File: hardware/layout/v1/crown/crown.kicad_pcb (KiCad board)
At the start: 4 copper layers, 34 x 34 mm, 47 parts, among them J1 Main board, J10 DOME_SOCKET, J2 XD_North, J3 XD_East, J4 XD_South, J5 XD_West, J6 PIEZO_NE, J7 PIEZO_NW, J8 PIEZO_SW, J9 PIEZO_SE, U1 SN74LVC2G04DBVR, U2 CD4052BM96, U3 TLV9062IDR, U4 LM393DR2G, U5 TLV9062IDR, U6 MMC5603NJ

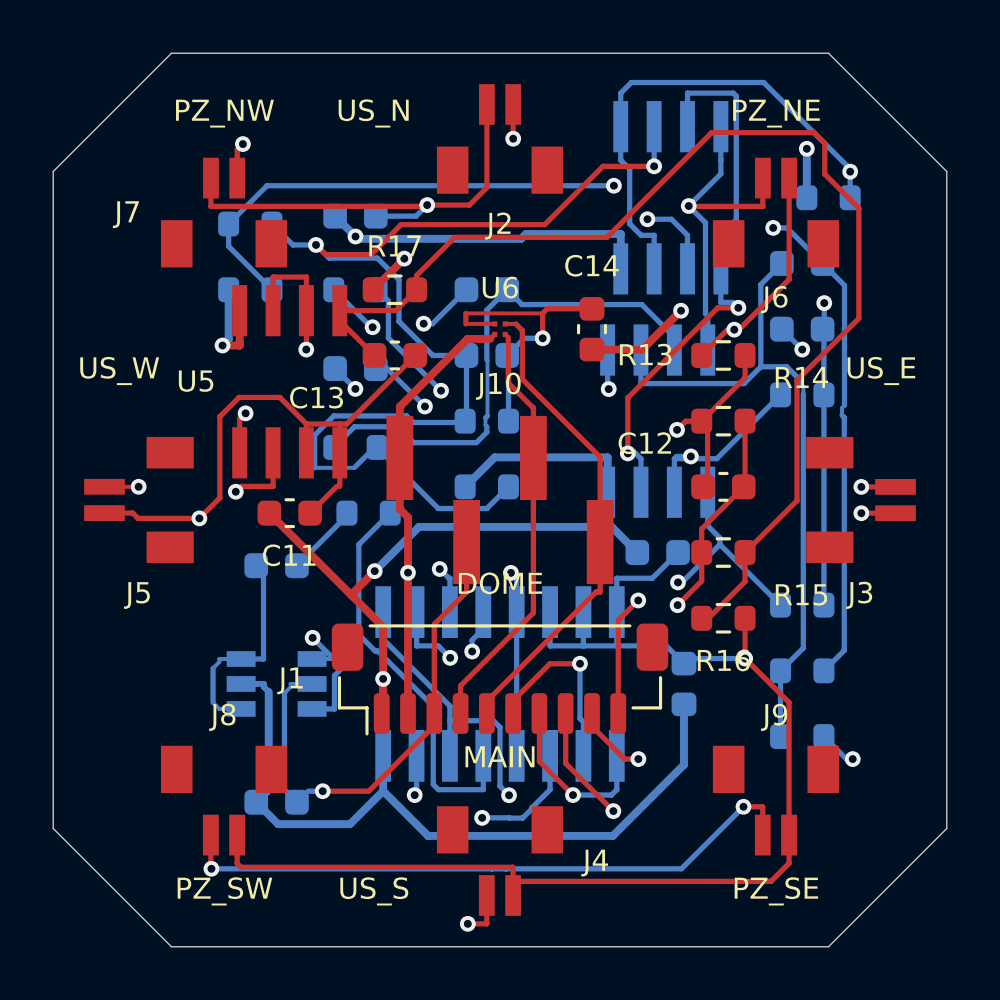
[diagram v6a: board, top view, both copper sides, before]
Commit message: Update enclosure dimensions, add power board, upgrade sensors, and redesign base bay for PMSA003I particulate module
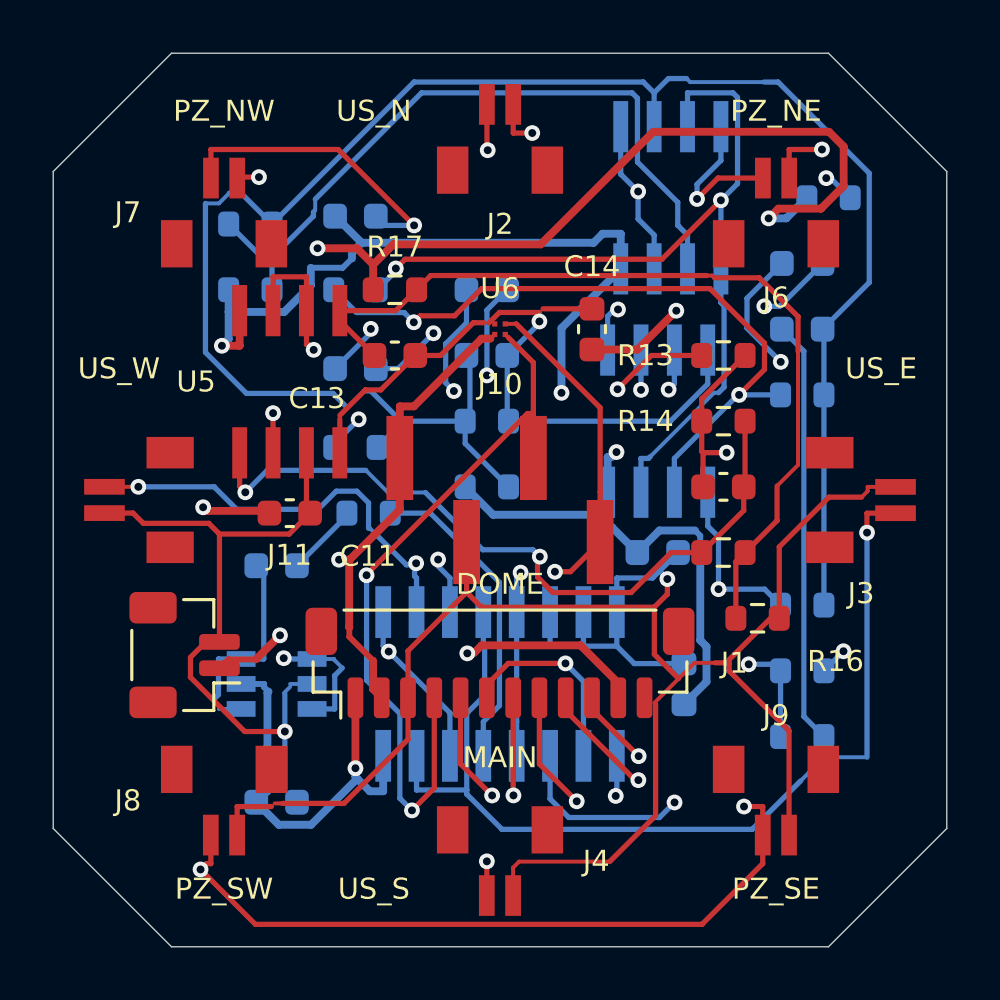
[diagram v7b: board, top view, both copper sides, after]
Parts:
- added J11: AUX 5V_HEAT, Connector_JST:JST_SH_BM02B-SRSS-TB_1x02-1MP_P1.00mm_Vertical, F.Cu at (5.00, -11.1)
- J1: footprint Connector_JST:JST_SH_BM10B-SRSS-TB_1x10-1MP_P1.00mm_Vertical -> Connector_JST:JST_SH_BM12B-SRSS-TB_1x12-1MP_P1.00mm_Vertical
- moved R16 1.30 mm to (26.8, -12.5)
- moved J1 0.60 mm to (17.0, -10.8)
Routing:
- net PIEZO_IN: track 85.6 -> 105.8 mm, vias 4 -> 5
- net +5V_HEAT: track 0.00 -> 17.3 mm, vias 0 -> 2
- net GND: track 131.6 -> 145.5 mm, vias 7 -> 6
- net +3V3: track 57.9 -> 71.1 mm
- net US_AMP1_FB: track 26.0 -> 39.2 mm, vias 0 -> 3
- net US_AMP2_IN: track 22.5 -> 35.7 mm
- net I2C_SDA: track 16.0 -> 28.4 mm, vias 0 -> 2
- net PIEZO_ENV: track 45.2 -> 33.3 mm
- net +5V: track 100.5 -> 90.2 mm, vias 4 -> 5
- net US_RX: track 47.3 -> 55.7 mm, vias 2 -> 3
- net I2C_SCL: track 18.4 -> 26.0 mm, vias 0 -> 2
- net XD_W: track 35.7 -> 41.4 mm
- net N$2: track 21.9 -> 16.2 mm, vias 2 -> 0
- net PIEZO_INV: track 37.4 -> 32.4 mm
- net US_AMP1_OUT: track 44.9 -> 39.9 mm, vias 3 -> 4
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
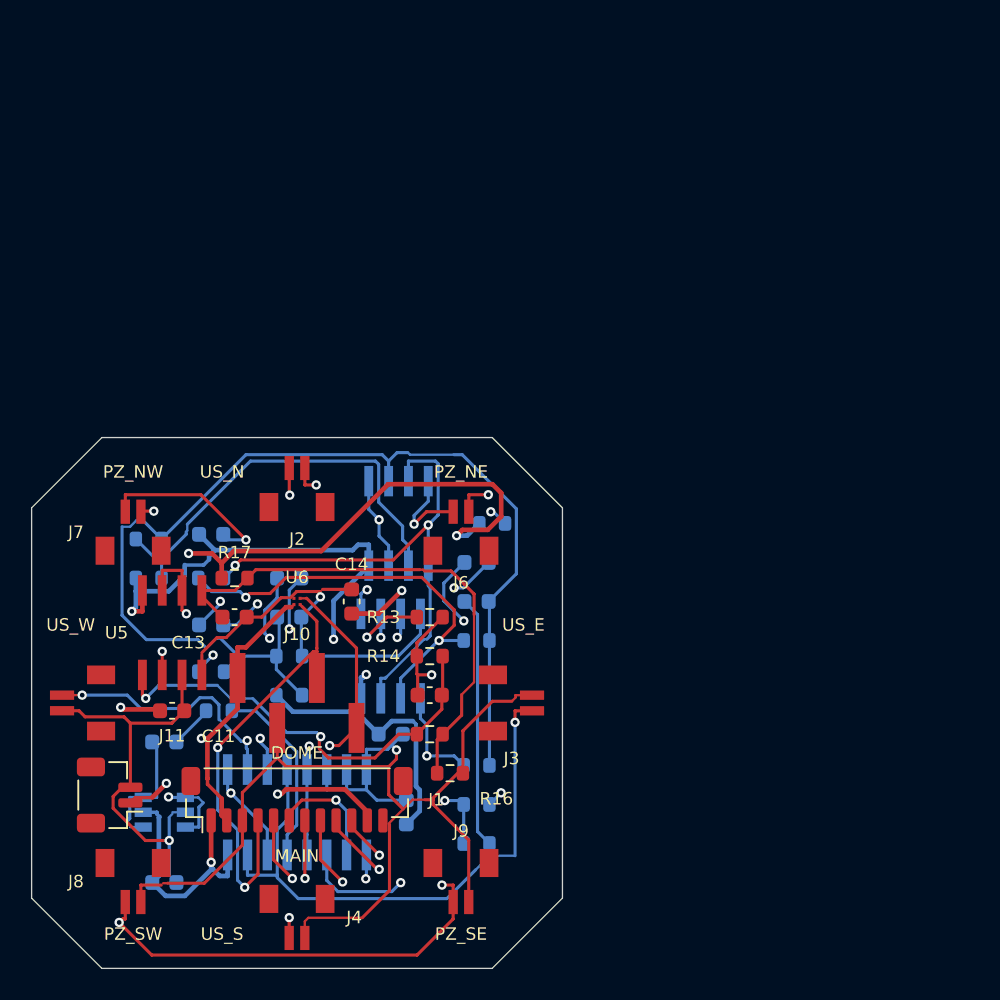
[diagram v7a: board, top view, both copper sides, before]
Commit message: Update documentation for 60V power system, STM32 crown board, 12V heaters, and expanded enclosure design
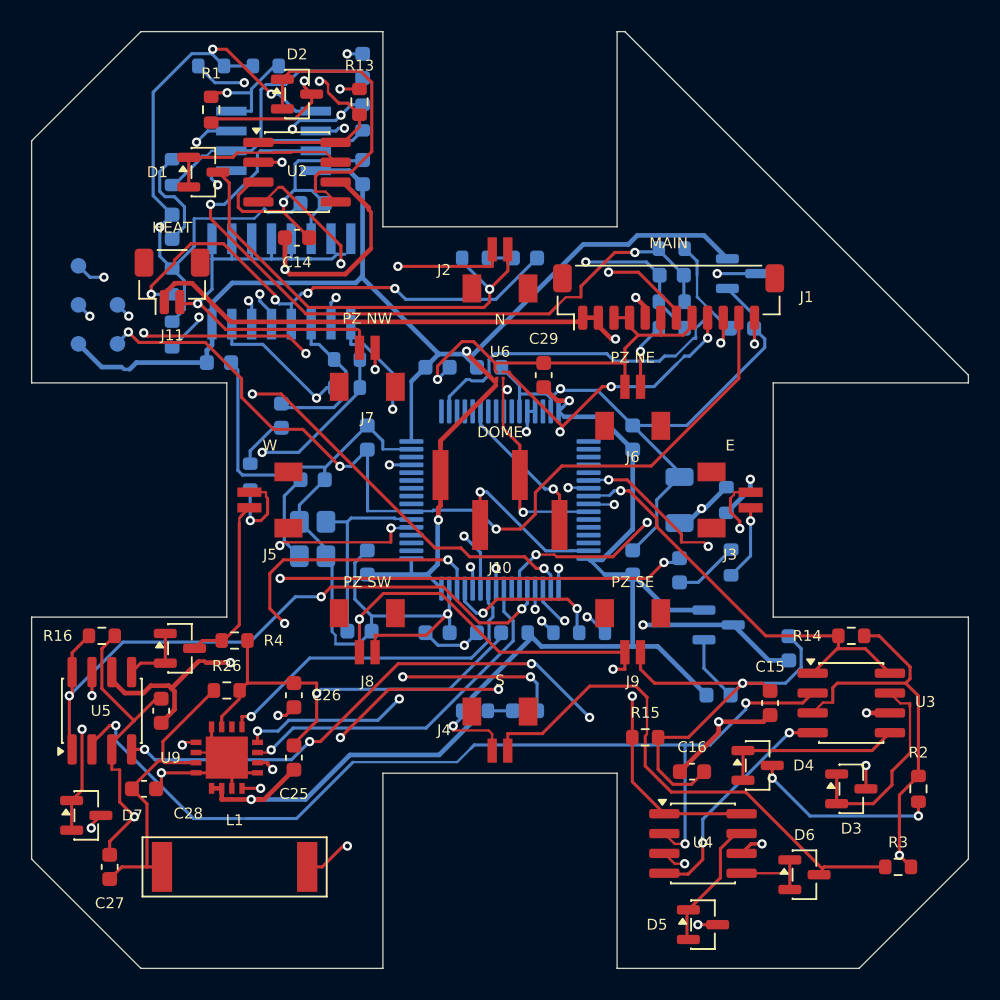
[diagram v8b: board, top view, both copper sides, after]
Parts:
- added C15: 1u 50V, Capacitor_SMD:C_0603_1608Metric, F.Cu at (47.3, -17.0)
- added C16: 1u 50V, Capacitor_SMD:C_0603_1608Metric, F.Cu at (42.3, -12.6)
- added C17: 1u 50V, Capacitor_SMD:C_0603_1608Metric, F.Cu at (8.30, -16.5)
- added C18: 1u 50V, Capacitor_SMD:C_0603_1608Metric, B.Cu at (18.0, -49.0)
- added C19: 100n 50V, Capacitor_SMD:C_0603_1608Metric, B.Cu at (9.00, -47.5)
- added C20: 220p C0G 50V, Capacitor_SMD:C_0603_1608Metric, B.Cu at (21.2, -57.8)
- added C21: 22n 50V, Capacitor_SMD:C_0603_1608Metric, B.Cu at (41.0, -44.4)
- added C22: 1n 50V, Capacitor_SMD:C_0603_1608Metric, B.Cu at (45.5, -41.0)
- added C23: 100n 50V, Capacitor_SMD:C_0603_1608Metric, B.Cu at (21.2, -51.0)
- added C24: 100n 50V, Capacitor_SMD:C_0603_1608Metric, B.Cu at (12.0, -38.8)
- added C25: 100n 50V, Capacitor_SMD:C_0603_1608Metric, F.Cu at (16.8, -13.5)
- added C26: 1u 50V, Capacitor_SMD:C_0603_1608Metric, F.Cu at (16.8, -17.5)
- added C27: 470p C0G 50V, Capacitor_SMD:C_0603_1608Metric, F.Cu at (5.00, -6.50)
- added C28: 470p C0G 50V, Capacitor_SMD:C_0603_1608Metric, F.Cu at (7.20, -11.5)
- added C29: 100n 50V, Capacitor_SMD:C_0603_1608Metric, F.Cu at (32.8, -38.0)
- added C30: 10n 50V, Capacitor_SMD:C_0603_1608Metric, B.Cu at (31.6, -45.5)
- added C31: 10n 50V, Capacitor_SMD:C_0603_1608Metric, B.Cu at (41.5, -25.5)
- added C32: 10n 50V, Capacitor_SMD:C_0603_1608Metric, B.Cu at (31.6, -16.5)
- added C33: 10n 50V, Capacitor_SMD:C_0603_1608Metric, B.Cu at (16.0, -35.4)
- added D1: BAV99, Package_TO_SOT_SMD:SOT-23, F.Cu at (11.0, -51.0)
- added D2: BAV99, Package_TO_SOT_SMD:SOT-23, F.Cu at (17.0, -56.0)
- added D3: BAV99, Package_TO_SOT_SMD:SOT-23, F.Cu at (52.5, -11.5)
- added D4: BAV99, Package_TO_SOT_SMD:SOT-23, F.Cu at (46.5, -13.0)
- added D5: BAV99, Package_TO_SOT_SMD:SOT-23, F.Cu at (43.0, -2.80)
- added D6: BAV99, Package_TO_SOT_SMD:SOT-23, F.Cu at (49.5, -6.00)
- added D7: BAV99, Package_TO_SOT_SMD:SOT-23, F.Cu at (3.50, -9.80)
- added D8: BAV99, Package_TO_SOT_SMD:SOT-23, F.Cu at (9.50, -20.5)
- added D9: BAV99, Package_TO_SOT_SMD:SOT-23, B.Cu at (45.5, -44.5)
- added L1: 100uH, RF_Antenna:Coilcraft_MA5532-AE_RFID, F.Cu at (13.0, -6.50)
- added R18: 10k, Resistor_SMD:R_0603_1608Metric, B.Cu at (11.5, -57.8)
- added R19: 10k, Resistor_SMD:R_0603_1608Metric, B.Cu at (15.0, -57.8)
- added R20: 1k, Resistor_SMD:R_0603_1608Metric, B.Cu at (9.00, -51.0)
- added R21: 6k8, Resistor_SMD:R_0603_1608Metric, B.Cu at (21.2, -54.5)
- added R22: 1k, Resistor_SMD:R_0603_1608Metric, B.Cu at (41.0, -41.0)
- added R23: 4M7, Resistor_SMD:R_0603_1608Metric, B.Cu at (41.0, -42.7)
- added R24: 1k, Resistor_SMD:R_0603_1608Metric, B.Cu at (41.0, -46.1)
- added R25: 10k, Resistor_SMD:R_0603_1608Metric, B.Cu at (35.9, -21.5)
- added R26: 10k, Resistor_SMD:R_0603_1608Metric, F.Cu at (12.5, -17.8)
- added R27: 10R, Resistor_SMD:R_0603_1608Metric, B.Cu at (32.6, -21.5)
- added TP1: 3V3, TestPoint:TestPoint_Pad_D1.0mm, B.Cu at (3.00, -40.0)
- added TP2: SWDIO, TestPoint:TestPoint_Pad_D1.0mm, B.Cu at (3.00, -42.5)
- added TP3: SWCLK, TestPoint:TestPoint_Pad_D1.0mm, B.Cu at (3.00, -45.0)
- added TP4: NRST, TestPoint:TestPoint_Pad_D1.0mm, B.Cu at (5.50, -40.0)
- added TP5: GND, TestPoint:TestPoint_Pad_D1.0mm, B.Cu at (5.50, -42.5)
- added U10: XC6206P332MR, Package_TO_SOT_SMD:SOT-23, B.Cu at (44.0, -22.0)
- added U7: 74HC4052D, gateway_fp:TI_CD4052BM96_SOIC-16, B.Cu at (16.0, -44.0)
- added U8: TLV9062IDR, gateway_fp:TI_TLV9062IDR_SOIC-8, B.Cu at (15.5, -53.0)
- added U9: AS3935-BQFT, gateway_fp:ScioSense_AS3935_QFN-16, F.Cu at (12.5, -13.5)
- added Y1: 8MHz, Crystal:Crystal_SMD_3225-4Pin_3.2x2.5mm, B.Cu at (18.0, -27.5)
- C1, C14: value 100n 50V -> 1u 50V
- C11: value 100n 50V -> 33p C0G 50V; moved to B.Cu
- C12: value 18p C0G 50V -> 33p C0G 50V; moved to B.Cu
- C13: value 220n 50V -> 22u 25V; footprint Capacitor_SMD:C_0603_1608Metric -> Capacitor_SMD:C_1206_3216Metric; moved to B.Cu
- C2: value 100n 50V -> 10u 10V
- C6, C9: value 47n 50V -> 100n 50V
- C7: value 47n 50V -> 10u 10V
- C8: value 18p C0G 50V -> 1u 50V
- J11: value AUX 5V_HEAT -> AUX 12V_HEAT
- J2: value XD_North -> XD_N
- J3: value XD_East -> XD_E
- J4: value XD_South -> XD_S
- J5: value XD_West -> XD_W
- R1, R4: value 1k -> 330R; moved to F.Cu
- R10: value 100k -> 1M
- R11: value 10k -> 1M
- R12: value 4k7 -> 1M
- R13: value 1k -> 10k
- R14: value 100k -> 10k
- R16: value 20k -> 10k
- R17: value 100k -> 10R; moved to B.Cu
- R2, R3: value 10k -> 330R; moved to F.Cu
- R5, R8: value 1k -> 47k
- R6: value 22k -> 47k
- R7: value 10k -> 47k
- R9: value 22k -> 1M
- U1: value SN74LVC2G04DBVR -> STM32G431RBT6; footprint gateway_fp:TI_SN74LVC2G04_SOT-23-6 -> Package_QFP:LQFP-64_10x10mm_P0.5mm
- U2: value CD4052BM96 -> UCC27524ADR; footprint gateway_fp:TI_CD4052BM96_SOIC-16 -> Package_SO:SOIC-8_3.9x4.9mm_P1.27mm; moved to F.Cu
- U3: value TLV9062IDR -> UCC27524ADR; footprint gateway_fp:TI_TLV9062IDR_SOIC-8 -> Package_SO:SOIC-8_3.9x4.9mm_P1.27mm; moved to F.Cu
- U4: value LM393DR2G -> UCC27524ADR; footprint gateway_fp:ON_LM393DR2G_SOIC-8 -> Package_SO:SOIC-8_3.9x4.9mm_P1.27mm; moved to F.Cu
- U5: value TLV9062IDR -> UCC27524ADR; footprint gateway_fp:TI_TLV9062IDR_SOIC-8 -> Package_SO:SOIC-8_3.9x4.9mm_P1.27mm
- moved C1 42.7 mm to (48.5, -20.5), turned to 90 degrees
- moved R3 41.3 mm to (55.5, -6.50)
- moved U2 41.0 mm to (17.0, -51.0)
- moved R2 40.7 mm to (56.8, -11.5), turned to 90 degrees
- moved J1 40.0 mm to (40.8, -43.0)
- moved R1 38.5 mm to (11.5, -55.0), turned to 90 degrees
- moved R5 37.5 mm to (28.4, -45.5)
- moved C2 35.6 mm to (44.0, -17.5)
- moved R13 33.3 mm to (21.0, -55.5), turned to 90 degrees
- moved J11 33.1 mm to (9.00, -44.0), turned to 0 degrees
- moved R17 31.9 mm to (44.5, -30.0), turned to 90 degrees
- moved U3 29.7 mm to (52.5, -17.0)
- moved C13 29.5 mm to (41.5, -30.0), turned to 90 degrees
- moved U1 29.4 mm to (30.0, -30.0)
- moved U4 28.3 mm to (43.0, -8.00)
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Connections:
- C10 pad 1: +5V -> CROWN_NRST
- C11 pad 1: +5V -> XTAL_IN
- C12 pad 1: PIEZO_INV -> XTAL_OUT
- C12 pad 2: PIEZO_STG1 -> GND
- C13 pad 1: PIEZO_ENV -> VDRV
- C14 pad 1: +3V3 -> VDRV
- C2 pad 1: US_TX_DRV -> +3V3
- C2 pad 2: N$1 -> GND
- C3 pad 1: +5V -> +3V3
- C4 pad 1: US_VREF -> +3V3
- C5 pad 1: +5V -> +3V3
- C6 pad 1: US_RX_MUX -> +3V3
- C6 pad 2: US_AMP1_IN -> GND
- C7 pad 1: N$2 -> +3V3
- C7 pad 2: US_VREF -> GND
- C8 pad 1: US_AMP1_FB -> +3V3A
- C8 pad 2: US_AMP1_OUT -> GND
- C9 pad 1: US_AMP1_OUT -> +3V3A
- C9 pad 2: US_AMP2_IN -> GND
- J1 pad 1: +5V -> +12V_HEAT
- J1 pad 10: RAIN_ADC -> CROWN_IRQ
- J1 pad 11: +5V_HEAT -> CROWN_NRST
- J1 pad 12: GND -> CROWN_BOOT0
- J1 pad 2: +3V3 -> +12V_HEAT
- J1 pad 4: I2C_SDA -> GND
- J1 pad 5: I2C_SCL -> +5V
- J1 pad 6: US_SEL_A -> GND
- J1 pad 7: US_SEL_B -> I2C_SDA
- J1 pad 8: US_TX -> GND
- J1 pad 9: US_RX -> I2C_SCL
- J11 pad 1: +5V_HEAT -> +12V_HEAT
- J2 pad 1: XD_N -> XD_N_A
- J2 pad 2: GND -> XD_N_B
- J3 pad 1: XD_E -> XD_E_A
- J3 pad 2: GND -> XD_E_B
- J4 pad 1: XD_S -> XD_S_A
- J4 pad 2: GND -> XD_S_B
- J5 pad 1: XD_W -> XD_W_A
- J5 pad 2: GND -> XD_W_B
- R1 pad 1: N$1 -> XD_N_B
- R1 pad 2: US_TX_AC -> GND
- R10 pad 1: +5V -> XD_E_RX
- R10 pad 2: US_VTH -> US_VREF
- R11 pad 1: US_VTH -> XD_S_RX
- R12 pad 1: +3V3 -> XD_W_RX
- R12 pad 2: US_RX -> US_VREF
- R13 pad 1: PIEZO_IN -> XD_EN_N
- R13 pad 2: PIEZO_INV -> GND
- R14 pad 1: PIEZO_INV -> XD_EN_E
- R14 pad 2: PIEZO_STG1 -> GND
- R15 pad 1: PIEZO_STG1 -> XD_EN_S
- R15 pad 2: PIEZO_ENV -> GND
- R16 pad 1: PIEZO_ENV -> XD_EN_W
- R17 pad 1: +3V3 -> +12V_HEAT
- R17 pad 2: PIEZO_ENV -> VDRV
- R2 pad 1: +5V -> XD_E_B
- R2 pad 2: US_VREF -> GND
- R3 pad 1: US_VREF -> XD_S_B
- R4 pad 1: US_AMP1_IN -> XD_W_B
- R4 pad 2: US_VREF -> GND
- R5 pad 1: US_AMP1_FB -> XD_N_A
- R5 pad 2: N$2 -> XD_N_RXC
- R6 pad 1: US_AMP1_FB -> XD_E_A
- R6 pad 2: US_AMP1_OUT -> XD_E_RXC
- R7 pad 1: US_AMP2_IN -> XD_S_A
- R7 pad 2: US_VREF -> XD_S_RXC
- R8 pad 1: US_AMP2_FB -> XD_W_A
- R8 pad 2: US_VREF -> XD_W_RXC
- R9 pad 1: US_AMP2_FB -> XD_N_RX
- R9 pad 2: US_AMP2_OUT -> US_VREF
- U1 pad 1: US_TX -> +3V3
- U1 pad 2: GND -> (no net)
- U1 pad 3: US_TX -> (no net)
- U1 pad 4: US_TX_DRV -> (no net)
- U1 pad 5: +5V -> XTAL_IN
- U1 pad 6: US_TX_DRV -> XTAL_OUT
- U2 pad 1: XD_S -> XD_EN_N
- U2 pad 2: XD_W -> TX_P
- U2 pad 3: US_RX_MUX -> GND
- U2 pad 4: XD_E -> TX_N
- U2 pad 5: XD_N -> XD_N_OUT_B
- U2 pad 6: GND -> VDRV
- U2 pad 7: GND -> XD_N_OUT_A
- U2 pad 8: GND -> XD_EN_N
- U3 pad 1: US_AMP1_OUT -> XD_EN_E
- U3 pad 2: US_AMP1_FB -> TX_P
- U3 pad 3: US_AMP1_IN -> GND
- U3 pad 4: GND -> TX_N
- U3 pad 5: US_AMP2_IN -> XD_E_OUT_B
- U3 pad 6: US_AMP2_FB -> VDRV
- U3 pad 7: US_AMP2_OUT -> XD_E_OUT_A
- U3 pad 8: +5V -> XD_EN_E
- U4 pad 1: US_RX -> XD_EN_S
- U4 pad 2: US_VREF -> TX_P
- U4 pad 3: US_AMP2_OUT -> GND
- U4 pad 4: GND -> TX_N
- U4 pad 5: US_AMP2_OUT -> XD_S_OUT_B
- U4 pad 6: US_VTH -> VDRV
- U4 pad 7: US_RX -> XD_S_OUT_A
- U4 pad 8: +5V -> XD_EN_S
- U5 pad 1: PIEZO_STG1 -> XD_EN_W
- U5 pad 2: PIEZO_INV -> TX_P
- U5 pad 4: GND -> TX_N
- U5 pad 5: PIEZO_ENV -> XD_W_OUT_B
- U5 pad 6: RAIN_ADC -> VDRV
- U5 pad 7: RAIN_ADC -> XD_W_OUT_A
- U5 pad 8: +5V -> XD_EN_W
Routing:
- net GND: track 145.5 -> 307.2 mm, vias 6 -> 17
- net TX_P: track 0.00 -> 141.9 mm, vias 0 -> 6
- net VDRV: track 0.00 -> 133.8 mm, vias 0 -> 6
- net +3V3: track 71.1 -> 175.2 mm
- net TX_N: track 0.00 -> 101.9 mm, vias 0 -> 8
- net +3V3A: track 0.00 -> 65.6 mm, vias 0 -> 4
- net CROWN_NRST: track 0.00 -> 58.0 mm, vias 0 -> 3
- net XD_EN_N: track 0.00 -> 57.4 mm, vias 0 -> 2
- net US_RX: track 55.7 -> 0.00 mm, vias 3 -> 0
- net +5V: track 90.2 -> 34.6 mm, vias 5 -> 2
- net XD_E_RX: track 0.00 -> 53.0 mm, vias 0 -> 4
- net SWDIO: track 0.00 -> 47.6 mm, vias 0 -> 4
- net PIEZO_OUT: track 0.00 -> 47.2 mm, vias 0 -> 2
- net +12V_HEAT: track 0.00 -> 47.1 mm, vias 0 -> 2
- net CROWN_BOOT0: track 0.00 -> 47.0 mm, vias 0 -> 3
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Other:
- board size 34 x 34 mm -> 60 x 60 mm
- board text added: "E"
- board text added: "HEAT"
- board text added: "N"
- board text added: "PZ NE"
- board text added: "PZ NW"
- board text added: "PZ SE"
- board text added: "PZ SW"
- board text added: "S"
- board text added: "SWD"
- board text added: "W"
- board text removed: "PZ_NE"
- board text removed: "PZ_NW"
- board text removed: "PZ_SE"
- board text removed: "PZ_SW"
- board text removed: "US_E"
- board text removed: "US_N"
- board text removed: "US_S"
- board text removed: "US_W"
